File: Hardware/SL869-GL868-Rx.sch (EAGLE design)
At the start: 195 parts, among them Q1 IRLML6402, Q10 8MHz, Q2 BC847/BSS138, Q5 IRF7353D2, Q6 IRLML6401, Q7 IRLML6401, SW1 SWT7, U1 74LVC1G02GV, U10 MAX1555, U11 STM32F103RBT6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

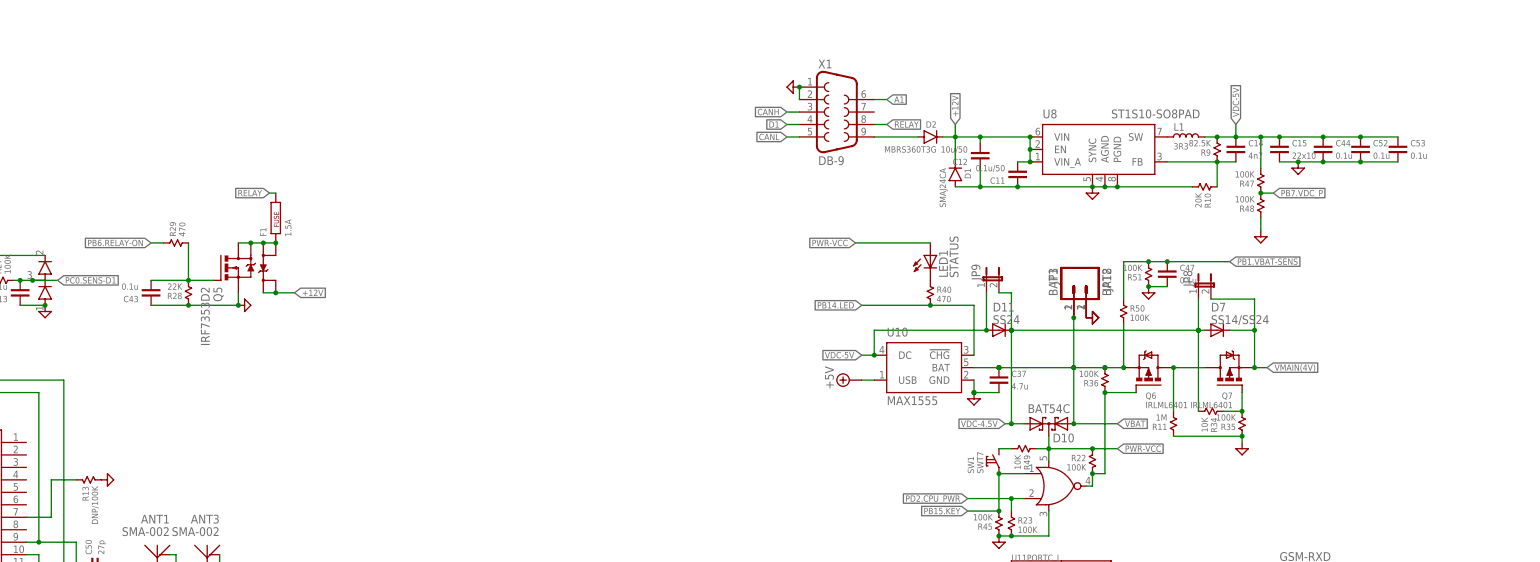
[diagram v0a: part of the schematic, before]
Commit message: Add remark for R9 and R13 values
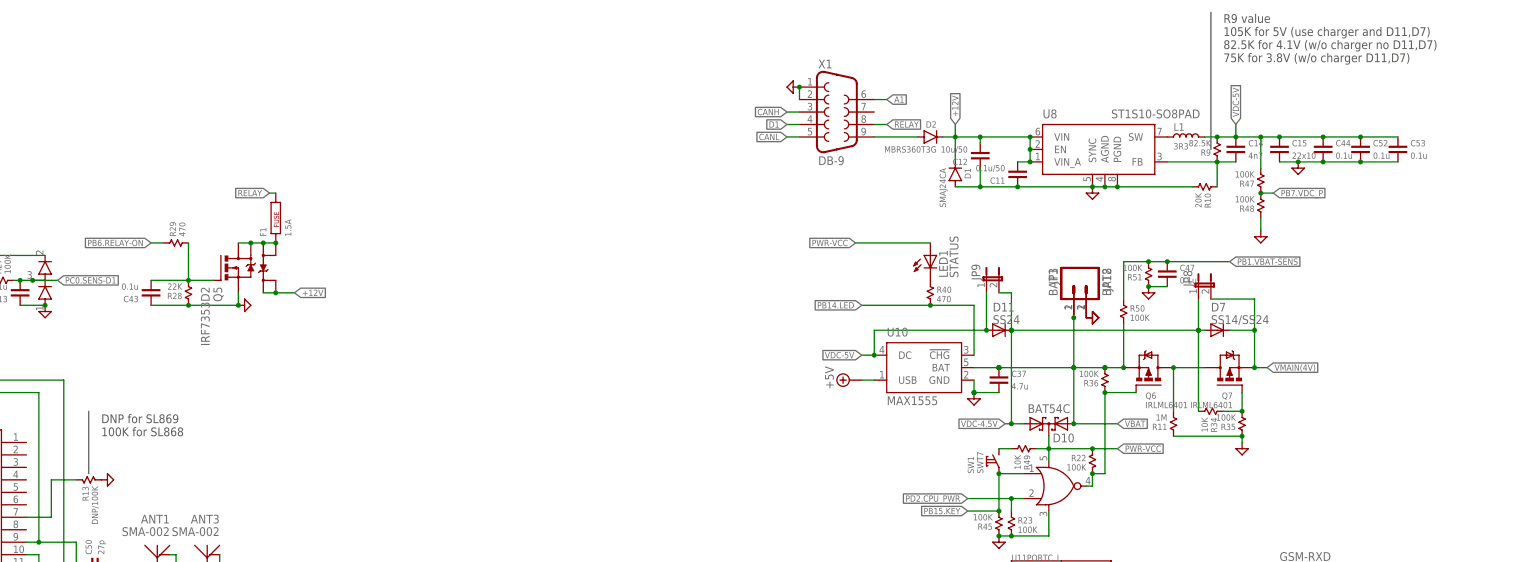
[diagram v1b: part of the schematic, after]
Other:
- note added: "DNP for SL869 100K for SL868"
- note added: "R9 value 105K for 5V (use charger and D11,D7) 82.5K for 4.1V (w/o charger no D11,D7) 75K for 3.8V (w/o charger D11,D7)"
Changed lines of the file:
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@@
 <setting verticaltext="up"/>
 </settings>
-<grid distance="0.05" unitdist="inch" unit="inch" style="lines" multiple="1" display="no" altdistance="0.01" altunitdist="inch" altunit="inch"/>
+<grid distance="0.1" unitdist="inch" unit="inch" style="lines" multiple="1" display="no" altdistance="0.01" altunitdist="inch" altunit="inch"/>
 <layers>
 <layer number="1" name="Top" color="4" fill="1" visible="no" active="no"/>
@@
 <wire x1="54.61" y1="194.31" x2="54.61" y2="191.77" width="0.1524" layer="97"/>
 <wire x1="54.61" y1="191.77" x2="57.15" y2="191.77" width="0.1524" layer="97"/>
+<text x="360.68" y="289.56" size="1.778" layer="97">R9 value
+105K for 5V (use charger and D11,D7)
+82.5K for 4.1V (w/o charger no D11,D7)
+75K for 3.8V (w/o charger D11,D7)</text>
+<wire x1="358.14" y1="271.78" x2="358.14" y2="299.72" width="0.1524" layer="97"/>
+<text x="132.08" y="213.36" size="1.778" layer="97">DNP for SL869
+100K for SL868</text>
+<wire x1="129.54" y1="205.74" x2="129.54" y2="218.44" width="0.1524" layer="97"/>
 </plain>
 <instances>
@@
 </schematic>
 </drawing>
+<compatibility>
+<note version="6.3" minversion="6.2.2" severity="warning">
+Since Version 6.2.2 text objects can contain more than one line,
+which will not be processed correctly with this version.
+</note>
+</compatibility>
 </eagle>

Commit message: Fix schematic/layout
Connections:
- removed net RXD1: U14.RXD_AUX(I)
- removed net TXD1: U14.TXD_AUX(O)
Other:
- moved on the sheet: GPS-RXD, GPS-TXD
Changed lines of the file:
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@@
 <?xml version="1.0" encoding="utf-8"?>
 <!DOCTYPE eagle SYSTEM "eagle.dtd">
-<eagle version="6.4">
+<eagle version="6.5.0">
 <drawing>
 <settings>
@@
 <setting verticaltext="up"/>
 </settings>
-<grid distance="0.1" unitdist="inch" unit="inch" style="lines" multiple="1" display="no" altdistance="0.01" altunitdist="inch" altunit="inch"/>
+<grid distance="0.05" unitdist="inch" unit="inch" style="lines" multiple="1" display="no" altdistance="0.01" altunitdist="inch" altunit="inch"/>
 <layers>
 <layer number="1" name="Top" color="4" fill="1" visible="no" active="no"/>
@@
 <instance part="PA2A" gate="G$1" x="284.48" y="154.94" rot="R90"/>
 <instance part="PA3A" gate="G$1" x="281.94" y="152.4" rot="R90"/>
-<instance part="GPS-RXD" gate="G$1" x="289.56" y="134.62"/>
-<instance part="GPS-TXD" gate="G$1" x="292.1" y="132.08"/>
+<instance part="GPS-RXD" gate="G$1" x="290.83" y="134.62"/>
+<instance part="GPS-TXD" gate="G$1" x="293.37" y="132.08"/>
 <instance part="GSM-RTS" gate="G$1" x="309.88" y="134.62" rot="R90"/>
 <instance part="GSM-RXD" gate="G$1" x="373.38" y="186.69"/>
@@
 <pinref part="JP3" gate="G$1" pin="1"/>
 <pinref part="SUPPLY48" gate="GND" pin="GND"/>
-</segment>
-<segment>
 <pinref part="JP18" gate="G$1" pin="2"/>
 <pinref part="SUPPLY49" gate="GND" pin="GND"/>
+<junction x="332.74" y="237.49"/>
 </segment>
 <segment>
@@
 <net name="PA10.GPS-TXD" class="0">
 <segment>
-<wire x1="312.42" y1="129.54" x2="292.1" y2="129.54" width="0.1524" layer="91"/>
+<wire x1="312.42" y1="129.54" x2="293.37" y2="129.54" width="0.1524" layer="91"/>
 <label x="288.29" y="129.54" size="1.27" layer="95" rot="R180" xref="yes"/>
 <pinref part="U11" gate="PORTA_H" pin="PA10"/>
 <pinref part="GPS-TXD" gate="G$1" pin="TP"/>
-<wire x1="292.1" y1="129.54" x2="288.29" y2="129.54" width="0.1524" layer="91"/>
-<junction x="292.1" y="129.54"/>
+<wire x1="293.37" y1="129.54" x2="288.29" y2="129.54" width="0.1524" layer="91"/>
+<junction x="293.37" y="129.54"/>
 </segment>
 <segment>
@@
 <net name="PA9.GPS-RXD" class="0">
 <segment>
-<wire x1="312.42" y1="132.08" x2="289.56" y2="132.08" width="0.1524" layer="91"/>
+<wire x1="312.42" y1="132.08" x2="290.83" y2="132.08" width="0.1524" layer="91"/>
 <label x="288.29" y="132.08" size="1.27" layer="95" rot="R180" xref="yes"/>
 <pinref part="U11" gate="PORTA_H" pin="PA9"/>
 <pinref part="GPS-RXD" gate="G$1" pin="TP"/>
-<wire x1="289.56" y1="132.08" x2="288.29" y2="132.08" width="0.1524" layer="91"/>
-<junction x="289.56" y="132.08"/>
+<wire x1="290.83" y1="132.08" x2="288.29" y2="132.08" width="0.1524" layer="91"/>
+<junction x="290.83" y="132.08"/>
 </segment>
 <segment>
@@
 <net name="GSM-ANT" class="0">
 <segment>
+<wire x1="96.52" y1="114.3" x2="114.3" y2="114.3" width="0.1524" layer="91"/>
+<label x="99.06" y="114.3" size="1.778" layer="95"/>
+<pinref part="U14" gate="G$1" pin="ANT"/>
 <wire x1="124.46" y1="114.3" x2="114.3" y2="114.3" width="0.1524" layer="91"/>
 <junction x="114.3" y="114.3"/>
 <pinref part="ANT2" gate="G$1" pin="ANT"/>
 <pinref part="ANT4" gate="G$1" pin="ANT"/>
-</segment>
-<segment>
-<wire x1="96.52" y1="114.3" x2="116.84" y2="114.3" width="0.1524" layer="91"/>
-<label x="99.06" y="114.3" size="1.778" layer="95"/>
-<pinref part="U14" gate="G$1" pin="ANT"/>
 </segment>
 </net>
@@
 <net name="GPS-RX1" class="0">
 <segment>
-<wire x1="68.58" y1="194.31" x2="62.23" y2="194.31" width="0.1524" layer="91"/>
+<wire x1="69.85" y1="194.31" x2="62.23" y2="194.31" width="0.1524" layer="91"/>
 <pinref part="JP2" gate="G$1" pin="3"/>
-</segment>
-<segment>
-<wire x1="69.85" y1="194.31" x2="68.58" y2="194.31" width="0.1524" layer="91"/>
 <wire x1="69.85" y1="194.31" x2="69.85" y2="204.47" width="0.1524" layer="91"/>
 <pinref part="U15" gate="G$1" pin="RX"/>
@@
 </segment>
 </net>
-<net name="N$2" class="0">
-<segment>
-<wire x1="138.43" y1="186.69" x2="139.7" y2="186.69" width="0.1524" layer="91"/>
-</segment>
-</net>
 <net name="N$3" class="0">
 <segment>
@@
 </segment>
 </net>
-<net name="RXD1" class="0">
-<segment>
-<pinref part="U14" gate="G$1" pin="RXD_AUX(I)"/>
-<wire x1="45.72" y1="73.66" x2="22.86" y2="73.66" width="0.1524" layer="91"/>
-<label x="22.86" y="73.66" size="1.27" layer="95" rot="R180" xref="yes"/>
-</segment>
-</net>
-<net name="TXD1" class="0">
-<segment>
-<pinref part="U14" gate="G$1" pin="TXD_AUX(O)"/>
-<wire x1="45.72" y1="71.12" x2="22.86" y2="71.12" width="0.1524" layer="91"/>
-<label x="22.86" y="71.12" size="1.27" layer="95" rot="R180" xref="yes"/>
-</segment>
-</net>
